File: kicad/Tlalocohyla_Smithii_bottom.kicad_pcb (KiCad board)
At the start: 2 copper layers, 215.7 x 90 mm, 38 parts

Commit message: Add filled zone
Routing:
- added copper zone on B.Cu, net (none)
- added copper zone on F.Cu, net (none)
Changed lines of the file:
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@@
   (gr_line (start 162.513285 75.07942) (end 162.543464 75.162337) (layer "Edge.Cuts") (width 0.15))
   (gr_arc (start 49.979881 50.373042) (mid 50.67877 49.462232) (end 51.816999 49.312382) (layer "Edge.Cuts") (width 0.15))
+  (zone (net 0) (net_name "") (layers F&B.Cu) (hatch edge 0.508)
+    (connect_pads (clearance 0.508))
+    (min_thickness 0.254) (filled_areas_thickness no)
+    (fill yes (thermal_gap 0.508) (thermal_bridge_width 0.508))
+    (polygon
+      (pts
+        (xy 260 140)
+        (xy 40 140)
+        (xy 40 40)
+        (xy 260 40)
+      )
+    )
+  )
 )

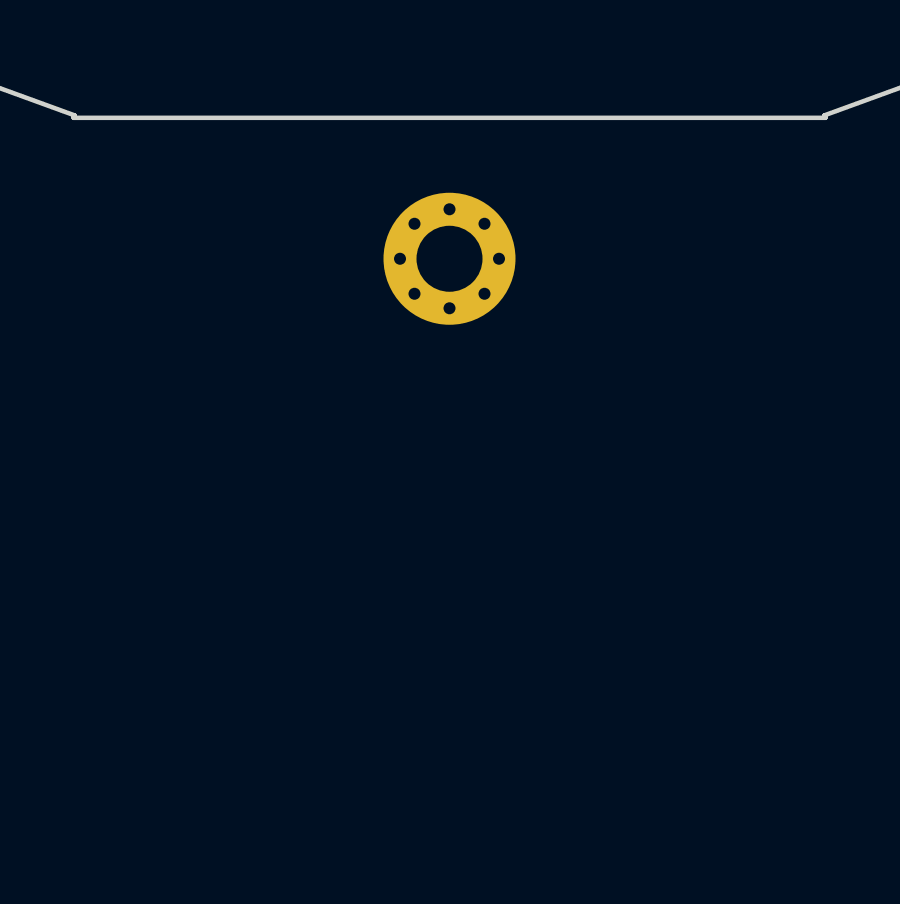
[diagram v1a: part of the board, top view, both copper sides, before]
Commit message: Change Xiao footprint
Reset and Battery plus
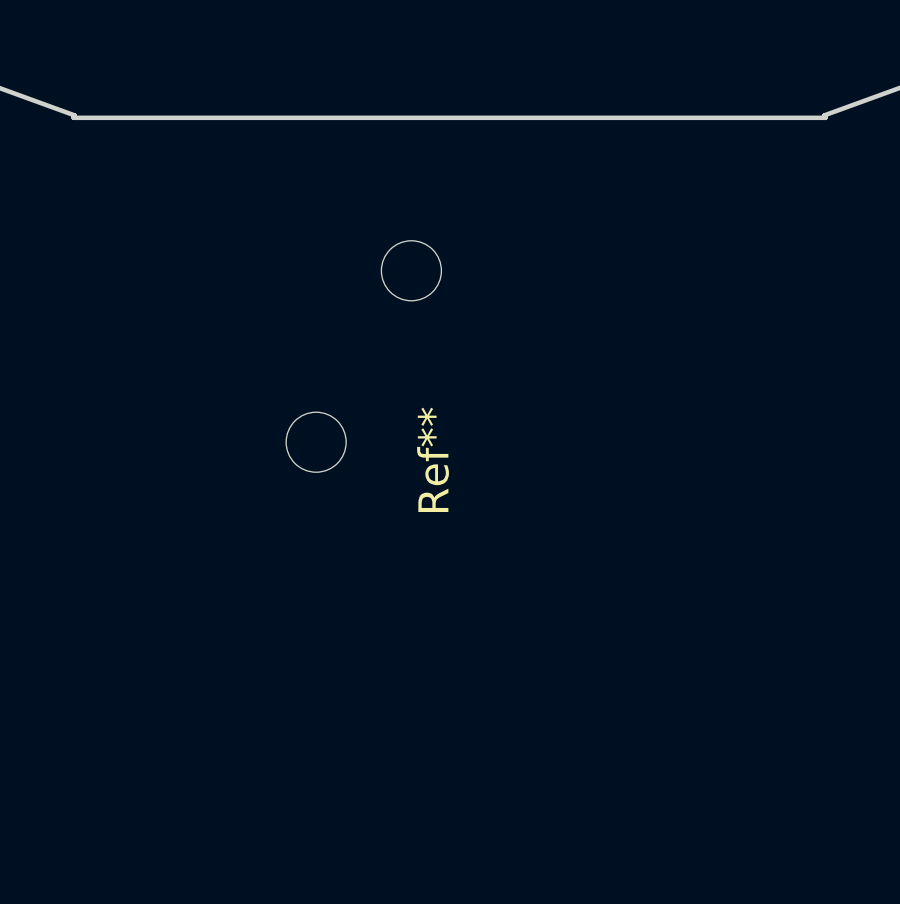
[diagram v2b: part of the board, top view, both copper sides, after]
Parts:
- removed the H** at (150.0, 79.9)
- Ref**: footprint Library:XiaoSimple -> Library:Xiao BLE pogo pins
- moved Ref** 13.5 mm to (150.0, 86.6), turned to 90 degrees
